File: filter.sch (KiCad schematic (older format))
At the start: 14 parts, among them U3 LM358

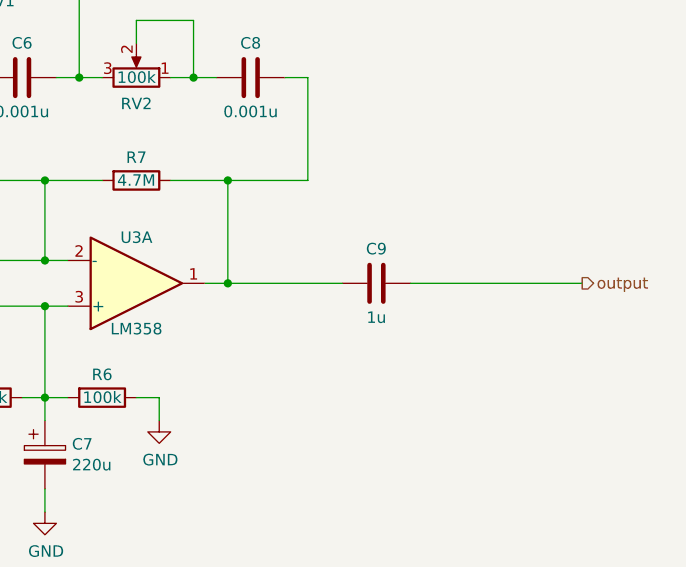
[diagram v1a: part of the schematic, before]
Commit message: Some suggestions for breadboard layout
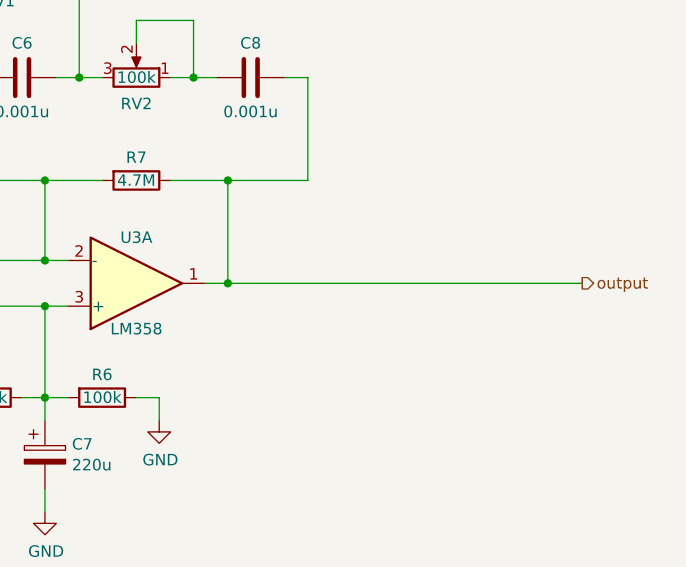
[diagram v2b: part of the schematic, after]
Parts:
- removed C9: 1u, Capacitor_THT:C_Rect_L7.2mm_W7.2mm_P5.00mm_FKS2_FKP2_MKS2_MKP2, symbol Device:C
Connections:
- net output: now also C8.1, R7.1, U3.1
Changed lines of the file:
@@
 	3250 3950 3850 3950
 Connection ~ 3850 3950
-Wire Wire Line
-	5150 4050 4650 4050
 Connection ~ 4650 4050
 Text HLabel 6200 4050 2    50   Output ~ 0
 output
-Wire Wire Line
-	6200 4050 5450 4050
 $Comp
 L Device:C C8
@@
 Wire Wire Line
 	3500 2700 3400 2700
-$Comp
-L Device:C C9
-U 1 1 5DACBD38
-P 5300 4050
-F 0 "C9" V 5150 4050 50  0000 C CNN
-F 1 "1u" V 5450 4050 50  0000 C CNN
-F 2 "Capacitor_THT:C_Rect_L7.2mm_W7.2mm_P5.00mm_FKS2_FKP2_MKS2_MKP2" H 5338 3900 50  0001 C CNN
-F 3 "~" H 5300 4050 50  0001 C CNN
-	1    5300 4050
-	0    1    1    0
-$EndComp
 Wire Wire Line
 	3400 4150 3850 4150
@@
 	3400 2700 3400 4150
 Connection ~ 3850 4150
+Wire Wire Line
+	4650 4050 6200 4050
 $EndSCHEMATC
